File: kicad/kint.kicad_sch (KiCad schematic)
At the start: 25 parts, among them J1 THUMB_RIGHT_SPC_KB600, J2 LEFT_13_LT, J3 TOP_LEFT, J4 TOP_RIGHT, J5 THUMB_LEFT_BAK, J6 THUMB_RIGHT_SPC, J7 RIGHT_13_DOWN, J8 THUMB_LEFT_BAK_KB600, U1 TEENSY_3.5_3.6

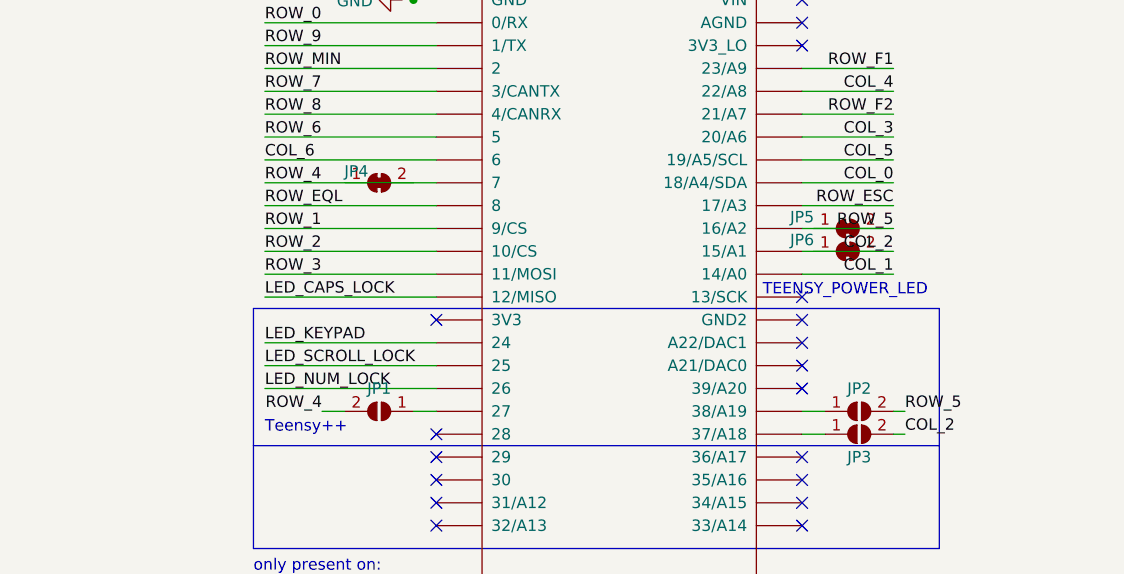
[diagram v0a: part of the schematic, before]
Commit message: Fix up board and schematic in KiCad
Not too bad, I think the merging was worth it
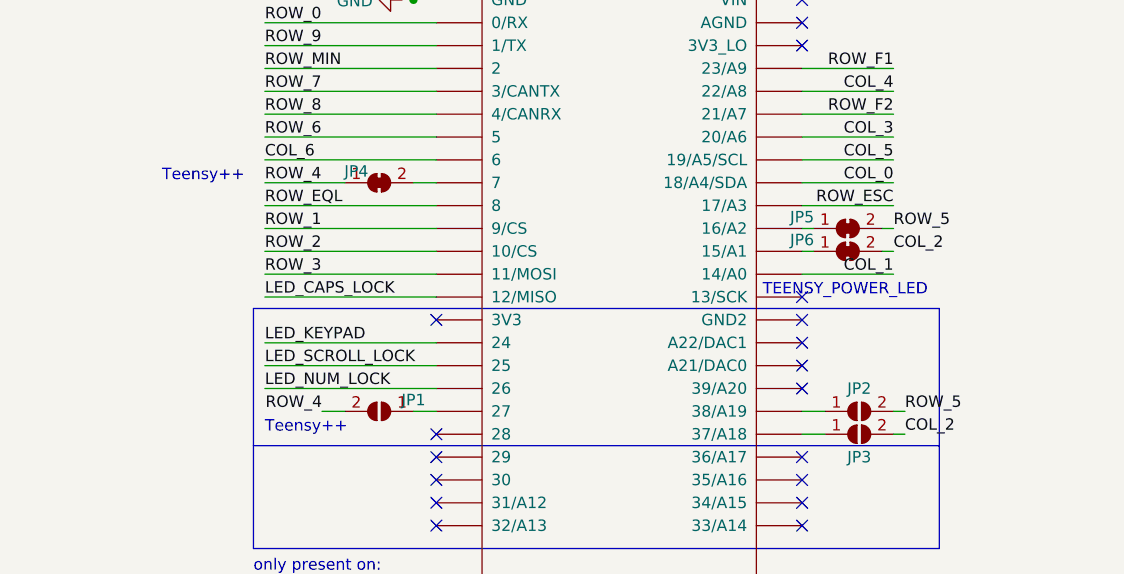
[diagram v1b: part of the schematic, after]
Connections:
- net COL_2: now also JP6.2 (B); no longer U1.15/A1
- net ROW_4: now also JP4.1 (A); no longer U1.7
- net ROW_5: now also JP5.2 (B); no longer U1.16/A2
- net at JP4.2 (B): now also U1.7
- net at JP5.1 (A): now also U1.16/A2
- net at JP6.1 (A): now also U1.15/A1
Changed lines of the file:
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@@
+    (stroke (width 0) (type default) (color 0 0 0 0))
+  )
+  (wire (pts (xy 129.54 63.5) (xy 132.08 63.5))
     (stroke (width 0) (type default) (color 0 0 0 0))
   )
@@
     (stroke (width 0) (type default) (color 0 0 0 0))
   )
+  (wire (pts (xy 173.99 68.58) (xy 172.72 68.58))
+    (stroke (width 0) (type default) (color 0 0 0 0))
+  )
   (polyline (pts (xy 238.76 111.76) (xy 238.76 153.67))
     (stroke (width 0) (type default) (color 0 0 0 0))
@@
     (stroke (width 0) (type default) (color 0 0 0 0))
   )
-  (wire (pts (xy 182.88 71.12) (xy 172.72 71.12))
+  (wire (pts (xy 182.88 71.12) (xy 181.61 71.12))
     (stroke (width 0) (type default) (color 0 0 0 0))
   )
@@
     (stroke (width 0) (type default) (color 0 0 0 0))
   )
-  (wire (pts (xy 132.08 63.5) (xy 113.03 63.5))
-    (stroke (width 0) (type default) (color 0 0 0 0))
-  )
   (wire (pts (xy 212.09 128.27) (xy 203.2 128.27))
     (stroke (width 0) (type default) (color 0 0 0 0))
@@
     (stroke (width 0) (type default) (color 0 0 0 0))
   )
+  (wire (pts (xy 173.99 71.12) (xy 172.72 71.12))
+    (stroke (width 0) (type default) (color 0 0 0 0))
+  )
   (polyline (pts (xy 13.97 105.41) (xy 53.34 105.41))
     (stroke (width 0) (type default) (color 0 0 0 0))
@@
     (stroke (width 0) (type default) (color 0 0 0 0))
   )
+  (wire (pts (xy 113.03 63.5) (xy 121.92 63.5))
+    (stroke (width 0) (type default) (color 0 0 0 0))
+  )
   (wire (pts (xy 132.08 53.34) (xy 113.03 53.34))
     (stroke (width 0) (type default) (color 0 0 0 0))
@@
     (stroke (width 0) (type default) (color 0 0 0 0))
   )
-  (wire (pts (xy 182.88 68.58) (xy 172.72 68.58))
+  (wire (pts (xy 182.88 68.58) (xy 181.61 68.58))
     (stroke (width 0) (type default) (color 0 0 0 0))
   )
@@
   (text "ROW_MIN" (at 26.67 85.09 180)
     (effects (font (size 1.27 1.27)) (justify right bottom))
+  )
+  (text "Teensy++" (at 101.6 63.5 0)
+    (effects (font (size 1.27 1.27)) (justify left bottom))
   )
   (text "ROW_6" (at 26.67 72.39 180)
@@
     (effects (font (size 1.27 1.27)) (justify left bottom))
   )
-  (label "COL_2" (at 182.88 71.12 180)
-    (effects (font (size 1.27 1.27)) (justify right bottom))
+  (label "COL_2" (at 182.88 71.12 0)
+    (effects (font (size 1.27 1.27)) (justify left bottom))
   )
   (label "ROW_F1" (at 50.8 29.21 180)
@@
     (effects (font (size 1.27 1.27)) (justify left bottom))
   )
-  (label "ROW_5" (at 182.88 68.58 180)
-    (effects (font (size 1.27 1.27)) (justify right bottom))
+  (label "ROW_5" (at 182.88 68.58 0)
+    (effects (font (size 1.27 1.27)) (justify left bottom))
   )
   (label "ROW_6" (at 50.8 72.39 180)
@@
   (symbol (lib_id "Jumper:SolderJumper_2_Open") (at 125.73 88.9 180) (unit 1)
     (in_bom yes) (on_board yes)
-    (property "Reference" "JP1" (id 0) (at 125.73 86.36 0))
+    (property "Reference" "JP1" (id 0) (at 129.54 87.63 0))
     (property "Value" "SolderJumper_2_Open" (id 1) (at 125.73 91.7956 0)
       (effects (font (size 1.27 1.27)) hide)
